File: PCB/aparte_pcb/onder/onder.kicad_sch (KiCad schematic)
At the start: 74 parts, among them J1 Conn_01x04_Socket, J2 Conn_01x10_Socket, Q1 NPN, Q2 NPN, Q3 NPN

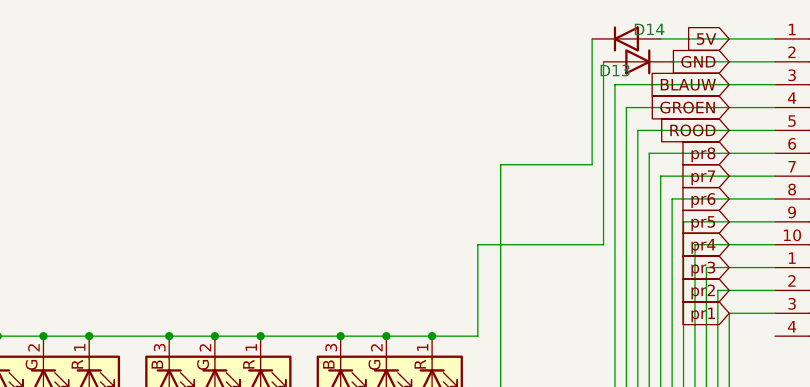
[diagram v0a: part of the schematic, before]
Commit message: schroef geaard
moet nog onderste schroef
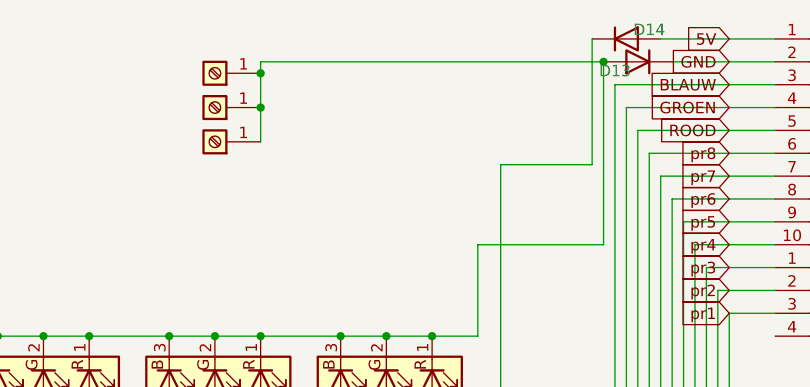
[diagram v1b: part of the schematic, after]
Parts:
- added J3, J4, J5: Screw_Terminal_01x01, MountingHole:MountingHole_4.3mm_M4_ISO7380_Pad, symbol Connector:Screw_Terminal_01x01
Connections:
- net at 10KΩ_1.2, 10KΩ_2.2, 10KΩ_3.2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: now also J3.1 (Pin_1), J4.1 (Pin_1), J5.1 (Pin_1)
